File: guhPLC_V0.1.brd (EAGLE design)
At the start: 156 x 86.5 mm, 170 parts, among them IC1 7812DT, K1 62104021021, K2 62104021021, K4 62101021021, K5 61900611021, Q1 BSS123, Q10 BSS123, Q11 BSS123, Q3 32.768k, Q4 BSS123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

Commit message: added pull ups for i2C changed the port for the 32kHz crystal at STM32
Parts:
- added R25, R26: 10k, resistor:R0603
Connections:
- net +3V3: now also R25.2, R26.2
- net OSCI: now also U$2.3; no longer U$2.5
- net OSCO: now also U$2.4; no longer U$2.6
- net SCL: now also R25.1
- net SDA: now also R26.1
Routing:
- net +3V3: track 482.8 -> 490.3 mm
- net SDA: track 120.3 -> 123.4 mm
- net SCL: track 119.5 -> 122.1 mm
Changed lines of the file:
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@@
 <element name="C16" library="resistor" package="C0805" value="100n" x="138.3" y="73.1" rot="R90"/>
 <element name="C17" library="resistor" package="C0805" value="100n" x="150.7" y="72.9" rot="R90"/>
+<element name="R25" library="resistor" package="R0603" value="10k" x="7.4" y="68.3" rot="R180"/>
+<element name="R26" library="resistor" package="R0603" value="10k" x="7.4" y="65.8" rot="R180"/>
 </elements>
 <signals>
@@
 <wire x1="11.3" y1="65.9" x2="11.2" y2="66" width="0.254" layer="16"/>
 <wire x1="11.2" y1="66" x2="11.8" y2="66.6" width="0.254" layer="16"/>
+<contactref element="R26" pad="1"/>
+<wire x1="8.25" y1="65.8" x2="8.35" y2="65.9" width="0.3048" layer="1"/>
+<wire x1="8.35" y1="65.9" x2="11.3" y2="65.9" width="0.3048" layer="1"/>
 </signal>
 <signal name="SCL">
@@
 <via x="10.7" y="67.8" extent="1-16" drill="0.6" shape="square"/>
 <wire x1="10.7" y1="67.8" x2="11.4" y2="67.2" width="0.254" layer="16"/>
+<contactref element="R25" pad="1"/>
+<wire x1="10.7" y1="67.8" x2="10.2" y2="68.3" width="0.3048" layer="1"/>
+<wire x1="10.2" y1="68.3" x2="8.25" y2="68.3" width="0.3048" layer="1"/>
 </signal>
 <signal name="OSCI">
-<contactref element="U$2" pad="5"/>
 <contactref element="Q3" pad="2"/>
 <contactref element="C4" pad="1"/>
-<wire x1="112.85" y1="49.25" x2="111.95" y2="49.25" width="0.254" layer="1"/>
-<wire x1="111.95" y1="49.25" x2="110.5" y2="50.7" width="0.254" layer="1"/>
 <wire x1="110.5" y1="50.7" x2="107.5" y2="50.7" width="0.254" layer="1"/>
 <wire x1="107.5" y1="50.7" x2="104.4" y2="53.9" width="0.254" layer="1"/>
@@
 <wire x1="105.9" y1="54" x2="104.33" y2="54" width="0.254" layer="1"/>
 <wire x1="104.33" y1="54" x2="104.2" y2="53.87" width="0.254" layer="1"/>
+<contactref element="U$2" pad="3"/>
+<wire x1="112.85" y1="50.25" x2="110.95" y2="50.25" width="0.254" layer="1"/>
+<wire x1="110.95" y1="50.25" x2="110.5" y2="50.7" width="0.254" layer="1"/>
 </signal>
 <signal name="ADC2">
@@
 <wire x1="31.6" y1="35.2" x2="37.8" y2="29" width="0.8128" layer="16"/>
 <wire x1="8.235" y1="74.25" x2="8.235" y2="72.535" width="0.8128" layer="1"/>
-<wire x1="8.235" y1="72.535" x2="2.6" y2="68.1" width="0.8128" layer="1"/>
-<wire x1="2.6" y1="68.1" x2="2.6" y2="44.7" width="0.8128" layer="1"/>
+<wire x1="8.235" y1="72.535" x2="2.964896875" y2="68.3446" width="0.8128" layer="1"/>
+<wire x1="2.964896875" y1="68.3446" x2="2.6" y2="68" width="0.8128" layer="1"/>
+<wire x1="2.6" y1="68" x2="2.6" y2="65.8" width="0.8128" layer="1"/>
+<wire x1="2.6" y1="65.8" x2="2.6" y2="44.7" width="0.8128" layer="1"/>
 <wire x1="2.6" y1="44.7" x2="5" y2="42.1" width="0.8128" layer="1"/>
 <via x="5" y="42.1" extent="1-16" drill="0.5"/>
@@
 <wire x1="30.4" y1="66.85" x2="30.45" y2="66.9" width="0.254" layer="1"/>
 <wire x1="30.45" y1="66.9" x2="30.5" y2="66.9" width="0.254" layer="1"/>
+<contactref element="R25" pad="2"/>
+<contactref element="R26" pad="2"/>
+<wire x1="6.55" y1="68.3" x2="6.1054" y2="68.3446" width="0.3048" layer="1"/>
+<wire x1="6.1054" y1="68.3446" x2="2.964896875" y2="68.3446" width="0.3048" layer="1"/>
+<wire x1="6.55" y1="65.8" x2="2.6" y2="65.8" width="0.3048" layer="1"/>
 <wire x1="47.2" y1="56.7" x2="47.2" y2="57.25" width="0" layer="19" extent="1-1"/>
 <wire x1="45.629" y1="47.0836" x2="45.6" y2="47.1" width="0" layer="19" extent="1-1"/>
@@
 </signal>
 <signal name="OSCO">
-<contactref element="U$2" pad="6"/>
 <contactref element="Q3" pad="1"/>
 <contactref element="C5" pad="1"/>
-<wire x1="112.85" y1="48.75" x2="111.55" y2="48.75" width="0.254" layer="1"/>
-<wire x1="111.55" y1="48.75" x2="110.2" y2="50.1" width="0.254" layer="1"/>
 <wire x1="110.2" y1="50.1" x2="107.3" y2="50.1" width="0.254" layer="1"/>
 <wire x1="107.3" y1="50.1" x2="106.1" y2="51.3" width="0.254" layer="1"/>
@@
 <wire x1="104.1" y1="50" x2="104.1" y2="51.23" width="0.254" layer="1"/>
 <wire x1="104.1" y1="51.23" x2="104.2" y2="51.33" width="0.254" layer="1"/>
+<contactref element="U$2" pad="4"/>
+<wire x1="112.85" y1="49.75" x2="110.55" y2="49.75" width="0.254" layer="1"/>
+<wire x1="110.55" y1="49.75" x2="110.2" y2="50.1" width="0.254" layer="1"/>
 </signal>
 <signal name="N$1">

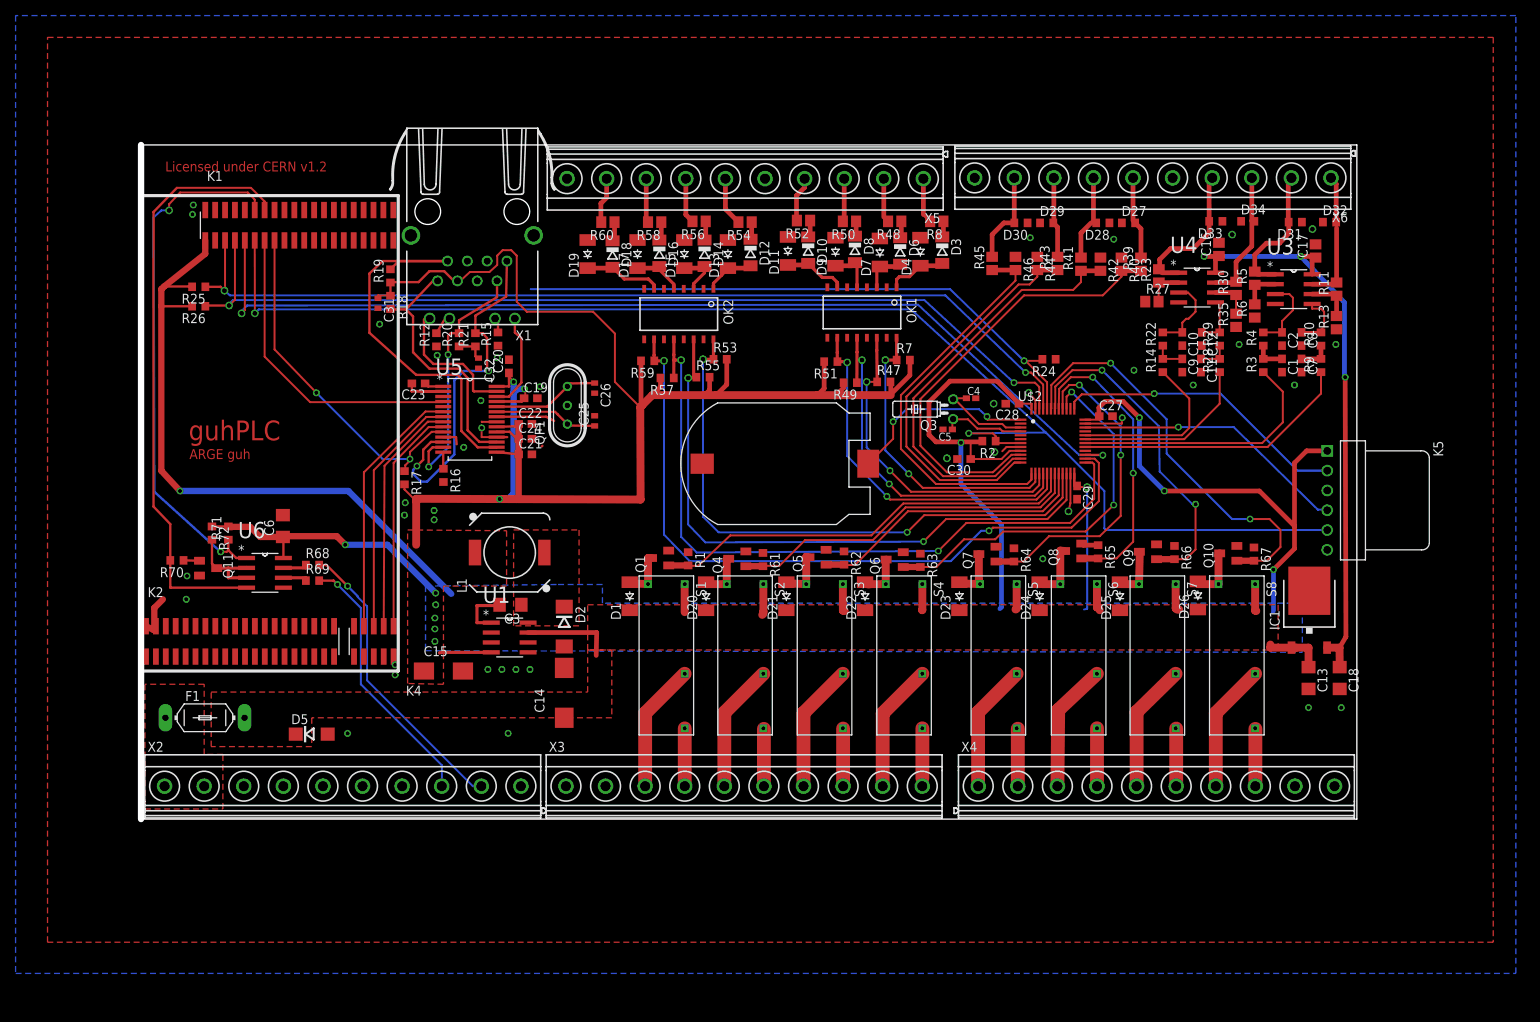
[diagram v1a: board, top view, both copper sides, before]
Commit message: Added License to README Minor bug fixes
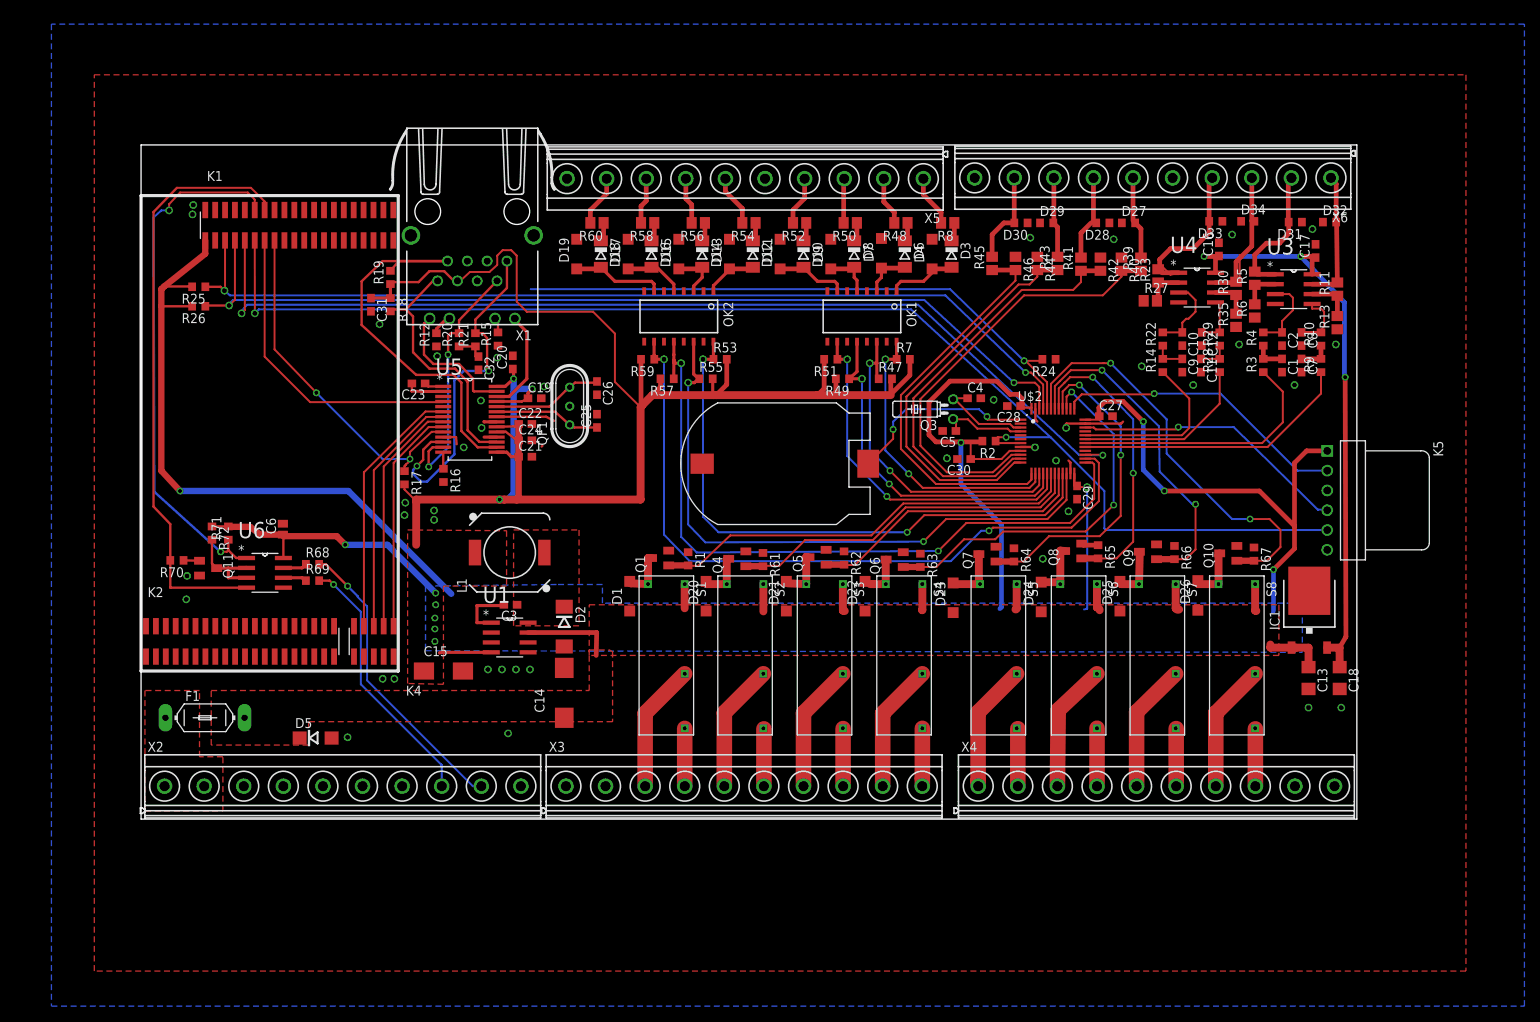
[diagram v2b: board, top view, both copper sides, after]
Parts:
- C16, C17: device resistor:C0805 -> resistor:C0603
- C25, C26, C31, C32: device resistor:C0402 -> resistor:C0603
- C3: device resistor:C1206 -> resistor:C0603
- C4, C5: value 10n -> 10p; device resistor:C0402K -> resistor:C0603
- C6: device resistor:C1206 -> resistor:C0504
- D1, D11, D13, D15, D17, D19, D20, D21, D22, D23, D24, D25, D26, D4, D7, D9: value CGRM4001-G -> 1N4148W-7-F; device diode:SOD-123_MINI-SMA -> guh:SOD123
- moved D4 1.53 mm to (101.5, 72.5)
- moved D18 1.50 mm to (59.0, 72.5)
- moved R8 1.41 mm to (103.5, 76.5)
- moved R60 1.40 mm to (58.5, 76.5)
- moved D19 1.40 mm to (55.9, 72.5)
- moved D3 1.30 mm to (104.0, 72.5)
- moved D17 1.20 mm to (62.5, 72.5)
- moved R49 1.12 mm to (90.0, 56.5)
- moved D11 1.08 mm to (82.0, 72.5)
- moved D16 1.00 mm to (65.5, 72.5)
- moved C31 0.92 mm to (29.5, 66.0)
- moved R58 0.91 mm to (65.0, 76.5)
- moved D23 0.82 mm to (104.2, 28.4)
- moved R48 0.82 mm to (97.5, 76.5)
- moved D10 0.78 mm to (85.0, 72.5)
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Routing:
- net GND: track 48.9 -> 37.7 mm
- net UC_NRST: track 179.0 -> 172.6 mm
- net IN3: track 49.3 -> 44.5 mm
- net AOUT3: track 17.2 -> 21.9 mm
- net +3V3: track 490.3 -> 494.7 mm
- net AOUT4: track 18.9 -> 22.6 mm
- net N$55: track 9.98 -> 11.8 mm
- net N$10: track 7.71 -> 9.24 mm
- net VCC: track 49.2 -> 47.7 mm
- net N$53: track 6.50 -> 7.70 mm
- net N$41: track 8.05 -> 9.22 mm
- net N$59: track 6.67 -> 7.85 mm
- net IN2: track 41.8 -> 42.9 mm
- net N$58: track 5.87 -> 6.96 mm
- net N$39: track 5.94 -> 6.79 mm
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
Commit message: Added 1-wire interface
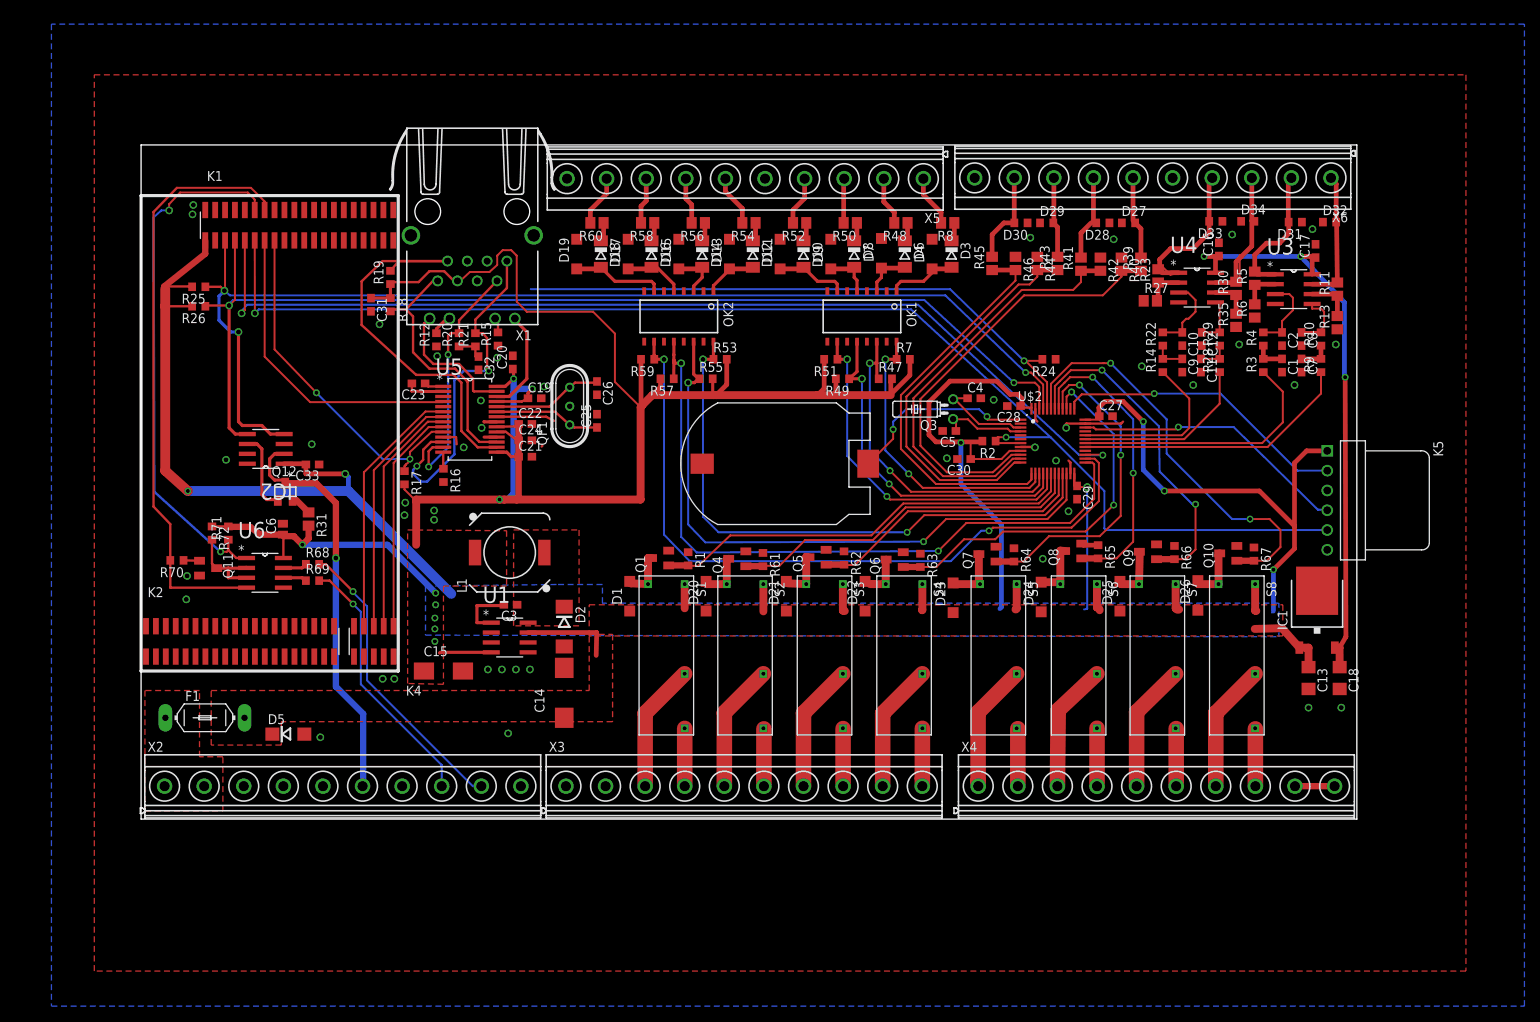
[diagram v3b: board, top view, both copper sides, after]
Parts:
- added C33: 100n, resistor:C0603
- added IC2: DS2482S-100SOI, guh:SOIC127P600X175-8N
- added Q12: FDN360P, transistor-power:SUPER-SOT3
- added R31: 10, resistor:R0805
- moved D5 3.54 mm to (18.9, 10.9)
- moved IC1 1.00 mm to (150.9, 26.8)
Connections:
- new net 1-WIRE: IC2.2, Q12.3, X2.6
- new net N$19: Q12.2, R31.1
- new net N$2: IC2.6, Q12.1
- net +3V3: now also C33.2, IC2.1, R31.2
- net GND: now also C33.1, IC2.3, IC2.7, IC2.8; no longer X2.6
- net SCL: now also IC2.4
- net SDA: now also IC2.5
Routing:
- net 1-WIRE: track 0.00 -> 52.3 mm, vias 0 -> 1
- net SCL: track 122.1 -> 147.4 mm, vias 2 -> 3
- net SDA: track 123.4 -> 141.7 mm
- net +3V3: track 494.7 -> 507.7 mm, vias 15 -> 16
- net N$2: track 0.00 -> 10.4 mm
- net GND: track 37.7 -> 42.7 mm, vias 41 -> 43
- net N$19: track 0.00 -> 2.69 mm
- net VCC: track 47.7 -> 49.8 mm
- net +12V: track 78.1 -> 77.1 mm
